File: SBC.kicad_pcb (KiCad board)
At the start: 6 copper layers, 85 x 54 mm, 286 parts, among them J1 USB_OTG, J2 Conn_ARM_JTAG_SWD_20, J3 USB_OTG, J4 Conn_02x25_Counter_Clockwise, U1 STPMIC1APQR, U2 IS43TR16640C-125JBL, U3 ECMF02-2AMX6, U4 ECMF02-2AMX6, U6 IS21ES08GA-JQLI-TR, U7 LAN8720A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

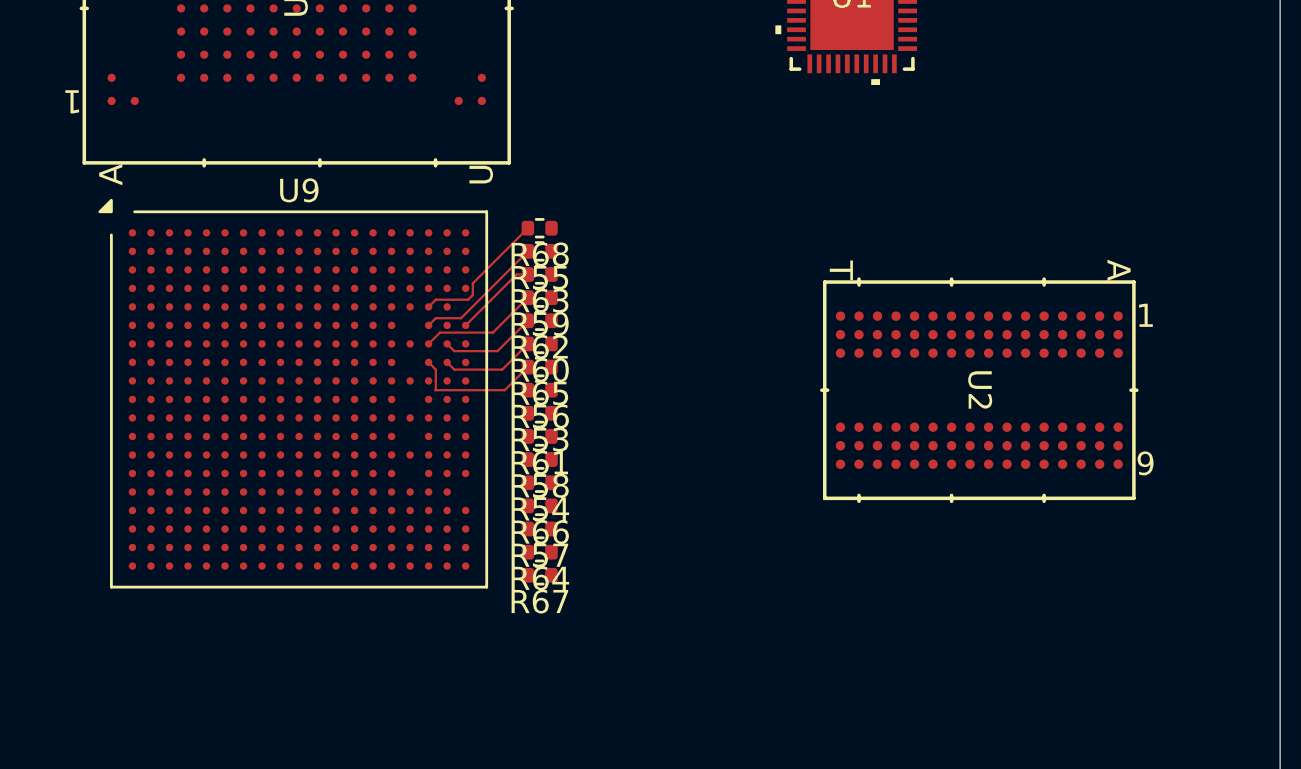
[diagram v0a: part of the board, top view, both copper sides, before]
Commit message: DDR Routing commenced
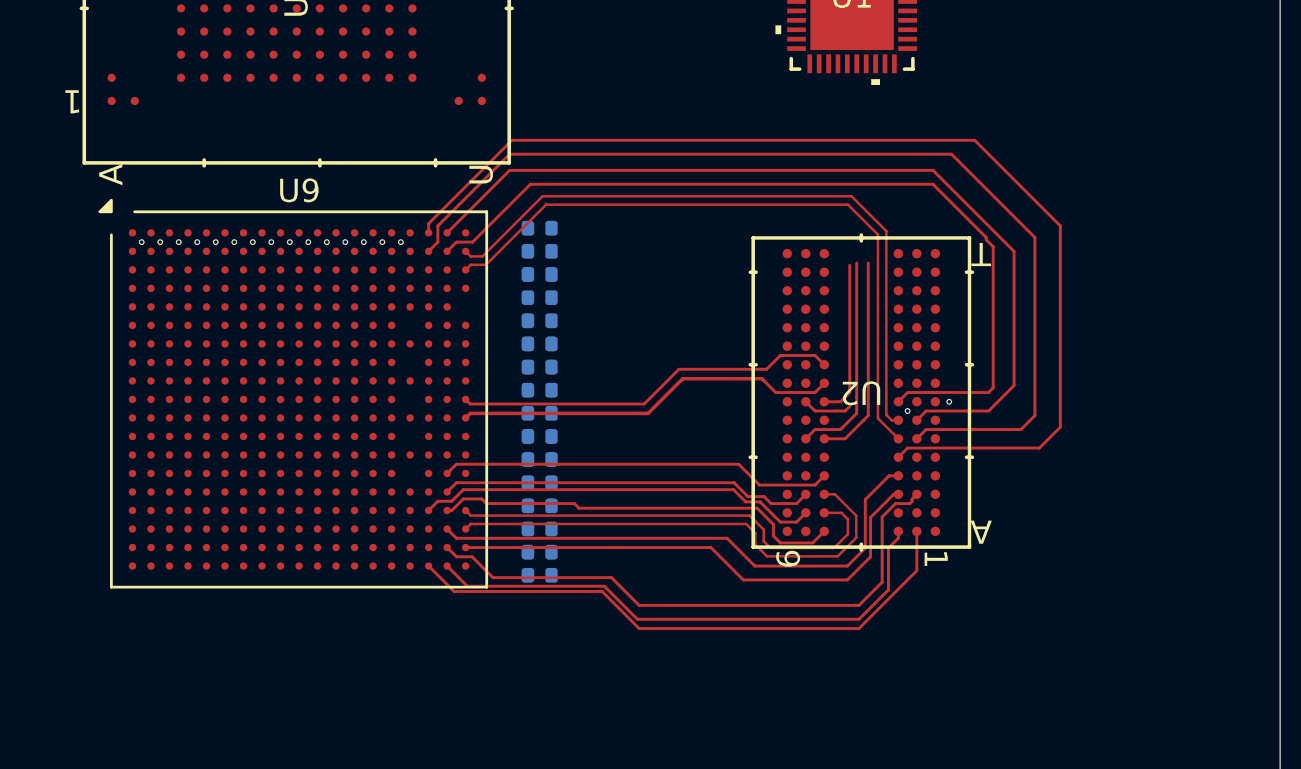
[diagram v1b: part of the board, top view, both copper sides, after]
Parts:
- R53, R54, R55, R56, R57, R58, R59, R60, R61, R62, R63, R64, R65, R66, R67, R68: moved to B.Cu
- moved U2 5.10 mm to (96.9, 67.1), turned to 180 degrees
- turned R53 to 0 degrees
- turned R54 to 0 degrees
- turned R55 to 0 degrees
- turned R56 to 0 degrees
- turned R57 to 0 degrees
- turned R58 to 0 degrees
- turned R59 to 0 degrees
- turned R60 to 0 degrees
- turned R61 to 0 degrees
- turned R62 to 0 degrees
- turned R63 to 0 degrees
- turned R64 to 0 degrees
- turned R65 to 0 degrees
- turned R66 to 0 degrees
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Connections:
- U2 pad A2: /MPU/DQ12 -> /MPU/DQ15
- U2 pad A3: /MPU/DQ11 -> /MPU/DQ12
- U2 pad A7: /MPU/DQ15 -> /MPU/DQ13
- U2 pad B8: /MPU/DQ14 -> /MPU/DQ9
- U2 pad C2: /MPU/DQ8 -> /MPU/DQ14
- U2 pad C3: /MPU/DQ13 -> /MPU/DQ11
- U2 pad C8: /MPU/DQ9 -> /MPU/DQ10
- U2 pad D7: /MPU/DQ10 -> /MPU/DQ8
- U2 pad E3: /MPU/DQ7 -> /MPU/DQ0
- U2 pad F7: /MPU/DQ5 -> /MPU/DQ4
- U2 pad F8: /MPU/DQ4 -> /MPU/DQ2
- U2 pad H3: /MPU/DQ0 -> /MPU/DQ7
- U2 pad H7: /MPU/DQ2 -> /MPU/DQ6
- U2 pad H8: /MPU/DQ6 -> /MPU/DQ5
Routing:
- net /MPU/DQ0: track 0.00 -> 47.0 mm
- net /MPU/DQ3: track 0.00 -> 43.1 mm
- net /MPU/DQ1: track 0.00 -> 37.7 mm
- net /MPU/DQ7: track 0.00 -> 36.4 mm
- net /MPU/DDR_DQS0_P: track 0.00 -> 28.7 mm
- net /MPU/DDR_DQS0_N: track 0.00 -> 28.5 mm
- net /MPU/DQ14: track 0.00 -> 25.0 mm
- net /MPU/DQ15: track 0.00 -> 25.0 mm
- net /MPU/DQ12: track 0.00 -> 23.3 mm
- net /MPU/DDR_DQM1: track 0.00 -> 23.0 mm
- net /MPU/DQ11: track 0.00 -> 21.9 mm
- net /MPU/DDR_DQS1_P: track 0.00 -> 20.9 mm
- net /MPU/DDR_DQS1_N: track 0.00 -> 19.5 mm
- net /MPU/DQ13: track 0.00 -> 17.8 mm
- net /MPU/DQ9: track 0.00 -> 17.4 mm
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
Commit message: DDR routing
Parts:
- R41, R45, R47: footprint Resistor_SMD:R_0201_0603Metric -> Resistor_SMD:R_0402_1005Metric; moved to B.Cu
- R69, R70, R71, R72, R73, R74, R75: moved to B.Cu
- moved R70 101.9 mm to (85.3, 54.2)
- moved R72 100.4 mm to (85.3, 60.2)
- moved R75 100.4 mm to (85.3, 66.3)
- moved R74 100.2 mm to (85.3, 65.3)
- moved R73 100.0 mm to (85.3, 64.3)
- moved R71 98.1 mm to (85.3, 72.1)
- moved R47 95.0 mm to (85.3, 63.3), turned to 180 degrees
- moved R41 94.8 mm to (85.3, 61.2), turned to 180 degrees
- moved R45 93.7 mm to (85.3, 75.1), turned to 180 degrees
- moved R69 81.2 mm to (99.3, 80.9), turned to 180 degrees
- moved R59 8.13 mm to (85.3, 55.2), turned to 180 degrees
- moved R55 8.04 mm to (85.3, 53.3), turned to 180 degrees
- moved R60 7.18 mm to (85.3, 58.2), turned to 180 degrees
- moved R62 7.18 mm to (85.3, 57.2), turned to 180 degrees
- moved R66 6.52 mm to (85.3, 78.1), turned to 180 degrees
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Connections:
- U2 pad F7: /MPU/DQ4 -> /MPU/DQ6
- U2 pad H7: /MPU/DQ6 -> /MPU/DQ4
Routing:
- net /MPU/DDR_DQM0: track 0.00 -> 32.4 mm
- net /MPU/DQ5: track 2.15 -> 29.4 mm
- net /MPU/DQ6: track 6.77 -> 29.4 mm
- net /MPU/DQ2: track 9.16 -> 29.9 mm
- net /MPU/DQ4: track 8.91 -> 26.2 mm
- net /MPU/A6: track 0.00 -> 13.8 mm, vias 0 -> 1
- net /MPU/A4: track 0.00 -> 11.9 mm, vias 0 -> 1
- net /MPU/DDR_BA1: track 0.00 -> 10.1 mm, vias 0 -> 1
- net /MPU/A8: track 0.00 -> 10.0 mm, vias 0 -> 1
- net /MPU/A1: track 0.00 -> 9.93 mm, vias 0 -> 1
- net /MPU/DDR_BA2: track 0.00 -> 9.09 mm, vias 0 -> 1
- net /MPU/DDR_CAS: track 0.00 -> 8.59 mm, vias 0 -> 1
- net /MPU/A5: track 0.00 -> 8.41 mm, vias 0 -> 1
- net /MPU/A15: track 0.00 -> 8.09 mm, vias 0 -> 1
- net /MPU/DDR_WE: track 0.00 -> 7.87 mm, vias 0 -> 1
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
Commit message: minor changes
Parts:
- moved R55 2.90 mm to (85.3, 56.2)
- moved R72 2.00 mm to (85.3, 62.2)
- moved R59 1.10 mm to (85.3, 54.1)
- moved R68 1.10 mm to (85.3, 55.1)
- moved R70 1.10 mm to (85.3, 53.1)
- moved R41 1.00 mm to (85.3, 60.2)
- moved R65 1.00 mm to (85.3, 61.2)
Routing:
- net Net-(U2-RESET#): track 0.00 -> 34.0 mm, vias 0 -> 1
- net Net-(U2-A13): track 0.00 -> 28.6 mm, vias 0 -> 1
- net Net-(U2-A9): track 0.00 -> 28.2 mm, vias 0 -> 1
- net Net-(U2-A7): track 0.00 -> 28.0 mm, vias 0 -> 1
- net Net-(U2-A3): track 0.00 -> 25.1 mm
- net Net-(U2-A0): track 0.00 -> 23.4 mm
- net Net-(U2-A2): track 0.00 -> 22.4 mm
- net Net-(U2-BA0): track 0.00 -> 20.5 mm
- net /MPU/DDR_RESETn: track 0.00 -> 15.1 mm, vias 0 -> 1
- net Net-(U2-BA2): track 0.00 -> 13.4 mm
- net Net-(U2-WE#): track 0.00 -> 13.4 mm
- net Net-(U2-CAS#): track 0.00 -> 13.2 mm
- net Net-(U2-A15): track 0.57 -> 11.5 mm
- net Net-(U2-A11): track 0.61 -> 10.8 mm
- net /MPU/A13: track 2.33 -> 12.4 mm
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
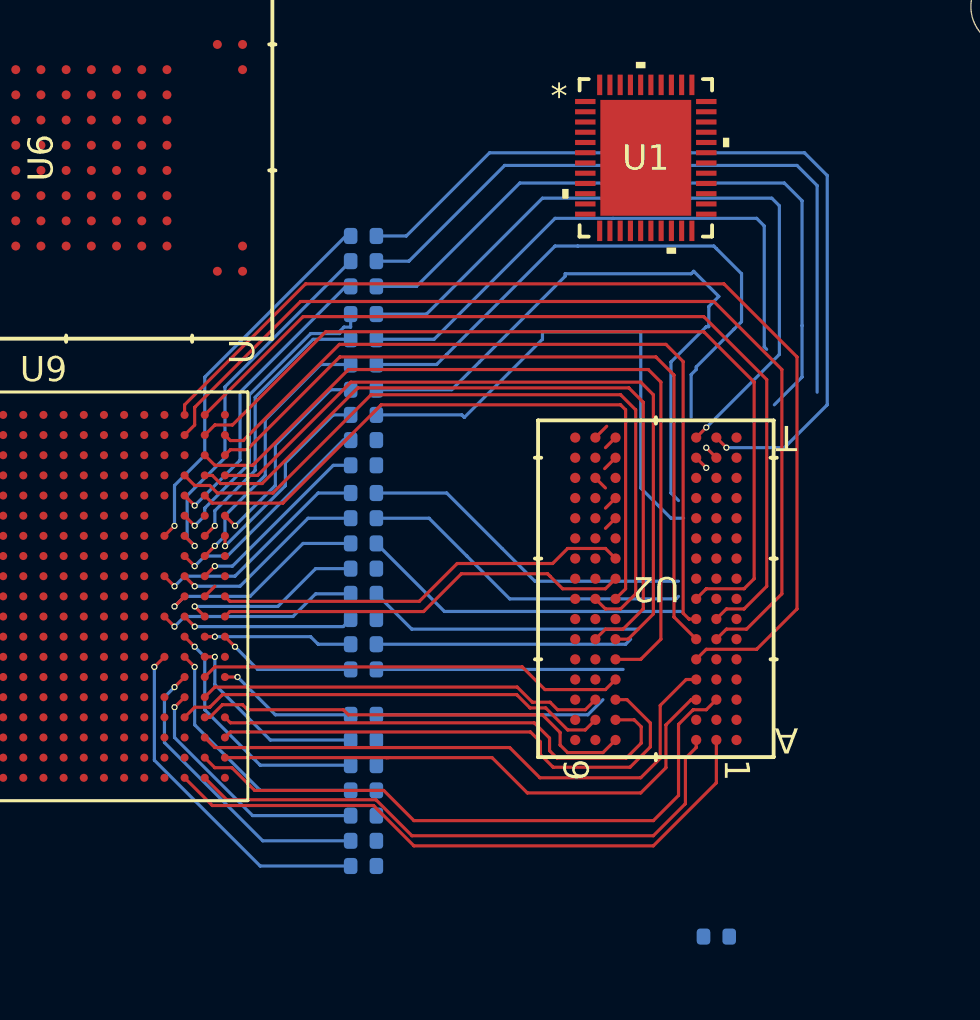
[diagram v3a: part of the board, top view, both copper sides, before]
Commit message: DDR complete needs polish
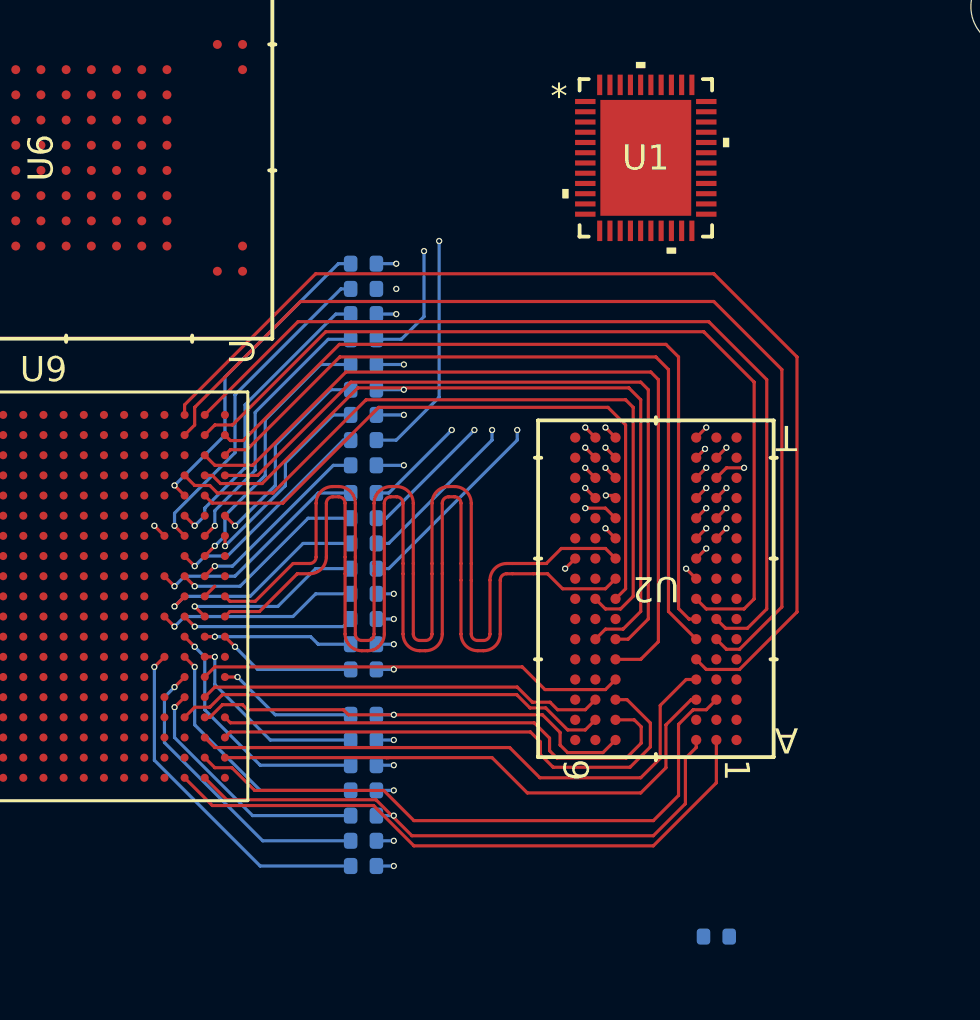
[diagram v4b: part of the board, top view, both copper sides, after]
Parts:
- removed R70: 33, Resistor_SMD:R_0402_1005Metric
- moved R59 1.10 mm to (85.3, 55.2)
- moved R68 0.90 mm to (85.3, 54.2)
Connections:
- U2 pad T2: Net-(U2-RESET#) -> /MPU/DDR_RESETn
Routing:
- net Net-(U2-CS#): track 0.00 -> 44.0 mm, vias 0 -> 2
- net Net-(U2-RESET#): track 34.0 -> 0.00 mm, vias 1 -> 0
- net /MPU/DDR_CLKN: track 16.6 -> 50.2 mm
- net /MPU/DDR_CLKP: track 16.6 -> 50.2 mm
- net Net-(U2-A5): track 0.00 -> 29.9 mm, vias 0 -> 2
- net Net-(U2-A6): track 0.00 -> 27.3 mm, vias 0 -> 2
- net Net-(U2-A8): track 0.64 -> 26.1 mm, vias 0 -> 2
- net Net-(U2-A4): track 0.57 -> 24.8 mm, vias 0 -> 2
- net Net-(U2-BA1): track 0.00 -> 21.1 mm, vias 0 -> 2
- net Net-(U2-RAS#): track 0.00 -> 20.7 mm, vias 0 -> 2
- net Net-(U2-A14): track 0.57 -> 20.9 mm, vias 0 -> 2
- net Net-(U2-A1): track 0.00 -> 20.3 mm, vias 0 -> 2
- net Net-(U2-BA0): track 20.5 -> 38.6 mm, vias 0 -> 2
- net /MPU/DDR_RESETn: track 15.1 -> 0.57 mm
- net Net-(U2-A13): track 28.6 -> 16.5 mm, vias 1 -> 2
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- added copper zone on In1.Cu, net GND

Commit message: DDR
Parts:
- removed R69: 33, Resistor_SMD:R_0402_1005Metric
- moved U1 7.06 mm to (95.0, 43.1)
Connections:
- net Net-(U2-A0) renamed /Memory/A0_R
- net Net-(U2-A1) renamed /Memory/A1_R
- net Net-(U2-A10/AP) renamed /Memory/A10_R
- net Net-(U2-A11) renamed /Memory/A11_R
- net Net-(U2-A12/BC#) renamed /Memory/A12_R
- net Net-(U2-A13) renamed /Memory/A13_R
- net Net-(U2-A14) renamed /Memory/A14_R
- net Net-(U2-A15) renamed /Memory/A15_R
- net Net-(U2-A2) renamed /Memory/A2_R
- net Net-(U2-A3) renamed /Memory/A3_R
- net Net-(U2-A4) renamed /Memory/A4_R
- net Net-(U2-A5) renamed /Memory/A5_R
- net Net-(U2-A6) renamed /Memory/A6_R
- net Net-(U2-A7) renamed /Memory/A7_R
- net Net-(U2-A8) renamed /Memory/A8_R
- net Net-(U2-A9) renamed /Memory/A9_R
- net Net-(U2-BA0) renamed /Memory/DDR_BA0_R
- net Net-(U2-BA1) renamed /Memory/DDR_BA1_R
- net Net-(U2-BA2) renamed /Memory/DDR_BA2_R
- net Net-(U2-CAS#) renamed /Memory/CAS_R
- net Net-(U2-CKE) renamed /Memory/CKE_R
- net Net-(U2-CS#) renamed /Memory/CS_R
- net Net-(U2-RAS#) renamed /Memory/RAS_R
- net Net-(U2-WE#) renamed /Memory/WE_R
- U2 pad K1: Net-(U2-ODT) -> /Memory/ODT
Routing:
- net /MPU/DQ10: track 16.2 -> 39.9 mm
- net /MPU/DQ9: track 17.4 -> 39.9 mm
- net /Memory/CS_R: track 44.0 -> 22.8 mm
- net /MPU/DDR_DQS1_P: track 20.9 -> 0.00 mm
- net /MPU/DDR_DQS1_N: track 19.5 -> 0.00 mm
- net /MPU/DDR_DQS0_P: track 30.6 -> 49.6 mm
- net /MPU/DDR_DQS0_N: track 30.7 -> 49.4 mm
- net /MPU/DQ13: track 17.8 -> 36.1 mm
- net /MPU/DQ8: track 17.0 -> 0.00 mm
- net /MPU/DQ7: track 35.6 -> 49.7 mm
- net /MPU/DQ1: track 36.4 -> 49.7 mm
- net /MPU/DQ14: track 25.0 -> 37.6 mm
- net /MPU/DQ3: track 40.3 -> 49.8 mm
- net /MPU/DQ11: track 21.9 -> 29.6 mm
- net /MPU/DQ15: track 25.0 -> 31.9 mm
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
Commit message: DDR routing
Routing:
- net /MPU/DQ4: track 25.5 -> 44.6 mm
- net /MPU/DQ5: track 28.6 -> 44.9 mm
- net /MPU/DQ2: track 29.3 -> 44.7 mm
- net /MPU/DDR_DQM0: track 31.7 -> 44.7 mm
- net /MPU/DQ6: track 28.9 -> 39.7 mm
- net /MPU/DQ12: track 29.5 -> 39.6 mm
- net /MPU/DQ11: track 29.6 -> 39.7 mm
- net /MPU/DDR_DQM1: track 29.9 -> 39.6 mm
- net /MPU/DQ15: track 31.9 -> 39.7 mm
- net /MPU/DQ3: track 49.8 -> 42.2 mm
- net /MPU/DQ0: track 49.8 -> 44.8 mm
- net /MPU/DQ7: track 49.7 -> 44.8 mm
- net /MPU/DQ1: track 49.7 -> 44.8 mm
- net /MPU/DDR_DQS0_N: track 49.4 -> 44.5 mm
- net /MPU/DDR_DQS0_P: track 49.6 -> 44.7 mm
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
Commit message: DDR Routing more
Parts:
- moved R53 6.71 mm to (84.1, 73.9)
- moved R54 2.51 mm to (84.1, 70.9)
- moved R47 2.00 mm to (84.1, 64.9)
- moved R58 2.00 mm to (84.1, 71.9)
- moved R73 2.00 mm to (84.1, 65.9)
- moved R74 2.00 mm to (84.1, 66.9)
- moved R75 2.00 mm to (84.1, 67.9)
- moved R41 2.00 mm to (84.1, 61.8)
- moved R55 2.00 mm to (84.1, 57.8)
- moved R59 2.00 mm to (84.1, 56.8)
- moved R60 2.00 mm to (84.1, 59.8)
- moved R62 2.00 mm to (84.1, 58.8)
- moved R63 2.00 mm to (84.1, 60.8)
- moved R65 2.00 mm to (84.1, 62.8)
- moved R68 2.00 mm to (84.1, 55.8)
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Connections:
- net /Memory/DDR_BA0_R renamed /Memory/BA0_R
- net /Memory/DDR_BA1_R renamed /Memory/BA1_R
- net /Memory/DDR_BA2_R renamed /Memory/BA2_R
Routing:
- net /Memory/BA0_R: track 36.8 -> 23.1 mm, vias 2 -> 1
- net /Memory/A3_R: track 32.5 -> 23.6 mm, vias 2 -> 1
- net /Memory/A15_R: track 11.1 -> 18.9 mm, vias 2 -> 1
- net /Memory/A13_R: track 16.5 -> 22.9 mm, vias 2 -> 1
- net /Memory/A9_R: track 18.5 -> 24.9 mm, vias 2 -> 1
- net /Memory/A7_R: track 19.4 -> 25.7 mm, vias 2 -> 1
- net /Memory/A0_R: track 17.7 -> 23.8 mm, vias 2 -> 1
- net /Memory/A5_R: track 29.9 -> 24.9 mm, vias 2 -> 1
- net /Memory/A11_R: track 14.9 -> 18.8 mm, vias 2 -> 1
- net /Memory/A14_R: track 20.9 -> 17.4 mm, vias 2 -> 1
- net /Memory/RAS_R: track 20.7 -> 23.6 mm, vias 2 -> 1
- net /Memory/CKE_R: track 12.8 -> 15.7 mm, vias 2 -> 1
- net /Memory/CAS_R: track 20.8 -> 23.4 mm, vias 2 -> 1
- net /Memory/WE_R: track 20.0 -> 22.5 mm, vias 2 -> 1
- net /Memory/BA2_R: track 19.6 -> 22.1 mm, vias 2 -> 1
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
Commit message: DDR done for now
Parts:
- moved CBUCK1IN1 161.5 mm to (52.0, 105.8)
- moved CBUCK2IN1 161.5 mm to (52.0, 108.3)
- moved CBUCK3IN1 161.5 mm to (52.0, 110.9)
- moved CBUCK4IN1 161.5 mm to (52.0, 113.4)
- moved CINTLDO1 161.5 mm to (39.3, 128.2)
- moved CLDO16IN1 161.5 mm to (39.3, 130.2)
- moved CLDO1OUT1 161.5 mm to (39.3, 132.2)
- moved CLDO25IN1 161.5 mm to (39.3, 134.1)
- moved CLDO2OUT1 161.5 mm to (39.3, 136.1)
- moved CLDO4OUT1 161.5 mm to (42.1, 128.2)
- moved CLDO5OUT1 161.5 mm to (42.1, 130.2)
- moved CLDO6OUT1 161.5 mm to (42.1, 132.2)
- moved CVIN1 161.5 mm to (42.1, 134.1)
- moved CVOUT3 161.5 mm to (60.0, 105.8)
- moved CVOUT4 161.5 mm to (60.0, 108.3)
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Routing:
- net /Memory/A10_R: track 14.0 -> 35.1 mm
- net /Memory/A12_R: track 13.3 -> 33.2 mm
- net /Memory/CKE_R: track 15.7 -> 35.1 mm
- net /Memory/A14_R: track 17.4 -> 33.5 mm
- net /Memory/A11_R: track 18.8 -> 34.9 mm
- net /Memory/A15_R: track 18.9 -> 31.0 mm
- net /Memory/RAS_R: track 23.6 -> 35.0 mm
- net /Memory/WE_R: track 22.5 -> 33.5 mm
- net /Memory/BA2_R: track 22.1 -> 32.5 mm
- net /Memory/CAS_R: track 23.4 -> 33.4 mm
- net /Memory/BA0_R: track 23.1 -> 32.9 mm
- net /Memory/A3_R: track 23.6 -> 33.3 mm
- net /Memory/A1_R: track 22.8 -> 30.7 mm
- net /Memory/BA1_R: track 22.3 -> 29.7 mm
- net /Memory/A0_R: track 23.8 -> 31.0 mm
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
